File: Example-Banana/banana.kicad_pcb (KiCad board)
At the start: 2 copper layers, 3 parts

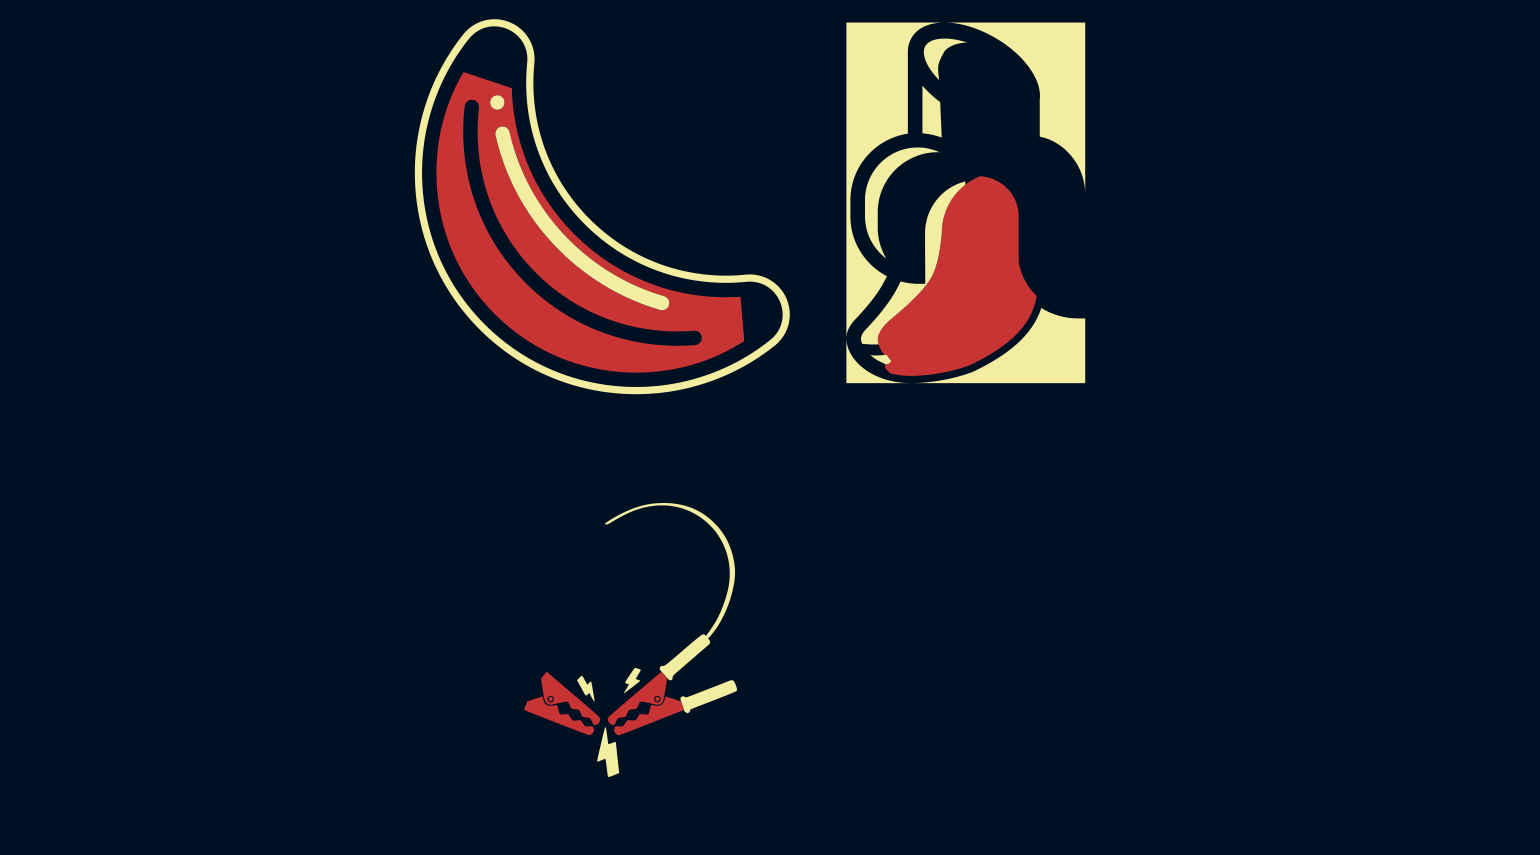
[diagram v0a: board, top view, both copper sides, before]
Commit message: More SVG in banana project
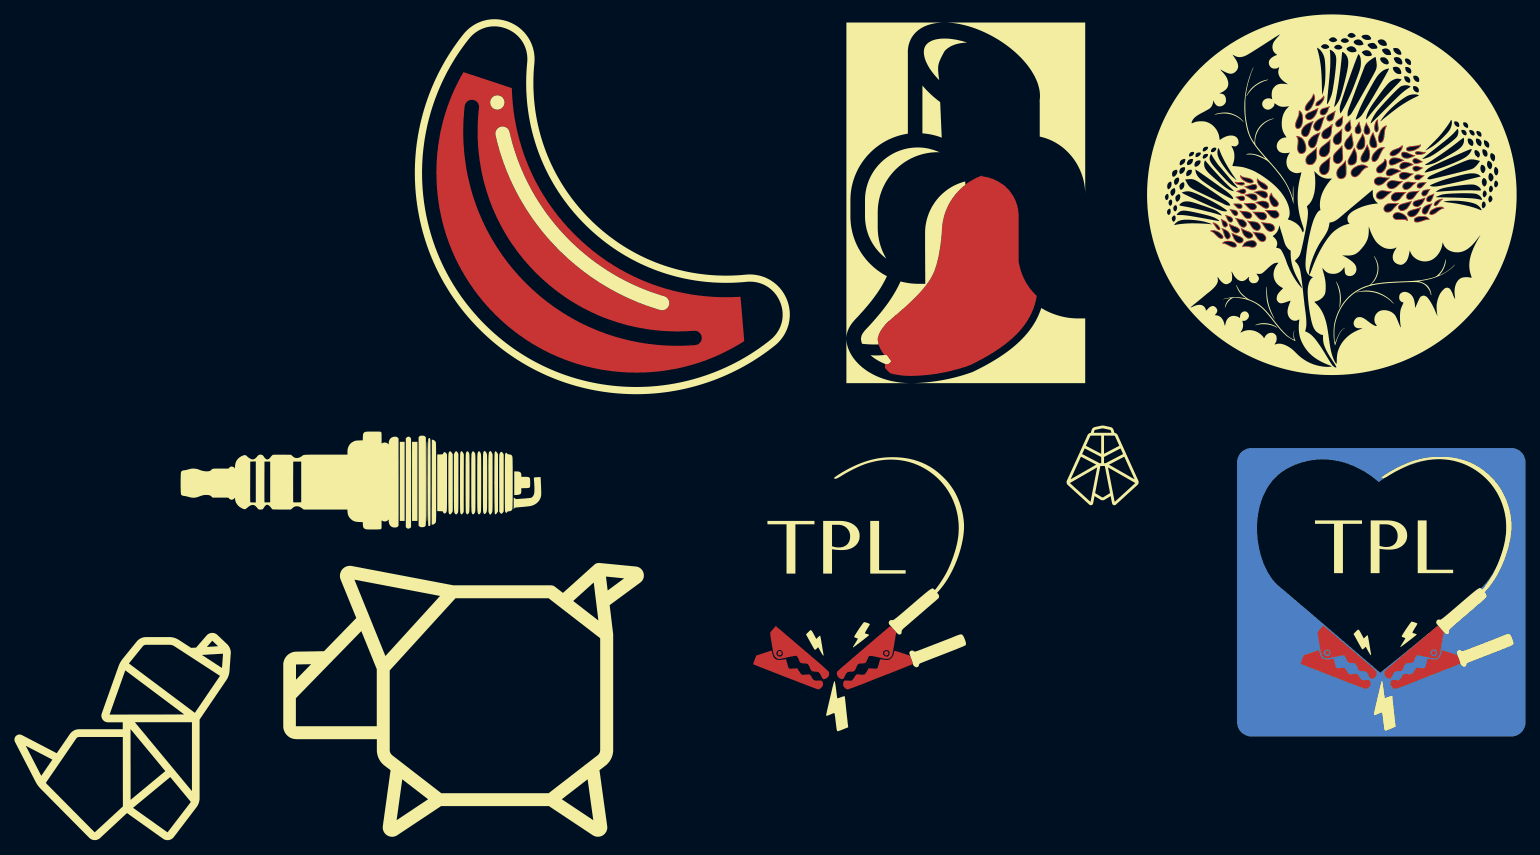
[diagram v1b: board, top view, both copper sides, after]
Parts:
- added svg2mod: G***, banana:thistle2, F.Cu at (231.1, 72.1)
- added svg2mod: G***, banana:lightning3, F.Cu at (238.0, 127.0)
- moved svg2mod 32.4 mm to (275.6, 12.7)
